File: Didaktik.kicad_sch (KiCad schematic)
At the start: 103 parts, among them J1 Conn_01x04_MountingPin, J2 AVR-ISP-6, SW1 SW_Push, SW10 SW_Push_45deg, SW11 SW_Push_45deg, SW12 SW_Push_45deg, SW13 SW_Push_45deg, SW14 SW_Push_45deg, SW15 SW_Push_45deg, SW16 SW_Push_45deg, SW17 SW_Push_45deg, SW18 SW_Push_45deg, SW19 SW_Push_45deg, SW2 SW_Push_45deg, SW20 SW_Push_45deg, SW21 SW_Push_45deg, SW22 SW_Push_45deg, SW23 SW_Push_45deg, SW24 SW_Push_45deg, SW25 SW_Push_45deg, SW26 SW_Push_45deg, SW27 SW_Push_45deg, SW28 SW_Push_45deg, SW29 SW_Push_45deg, SW3 SW_Push_45deg, SW30 SW_Push_45deg, SW31 SW_Push_45deg, SW32 SW_Push_45deg, SW33 SW_Push_45deg, SW34 SW_Push_45deg, SW35 SW_Push_45deg, SW36 SW_Push_45deg, SW37 SW_Push_45deg, SW38 SW_Push_45deg, SW39 SW_Push_45deg, SW4 SW_Push_45deg, SW40 SW_Push_45deg, SW41 SW_Push_45deg, SW5 SW_Push_45deg, SW6 SW_Push_45deg, SW7 SW_Push_45deg, SW8 SW_Push_45deg, SW9 SW_Push_45deg, U1 ATmega32U4-M, Y1 Crystal_GND24_Small

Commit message: added multi layout proto
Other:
- moved on the sheet: C1, C2, C5, C7, C8

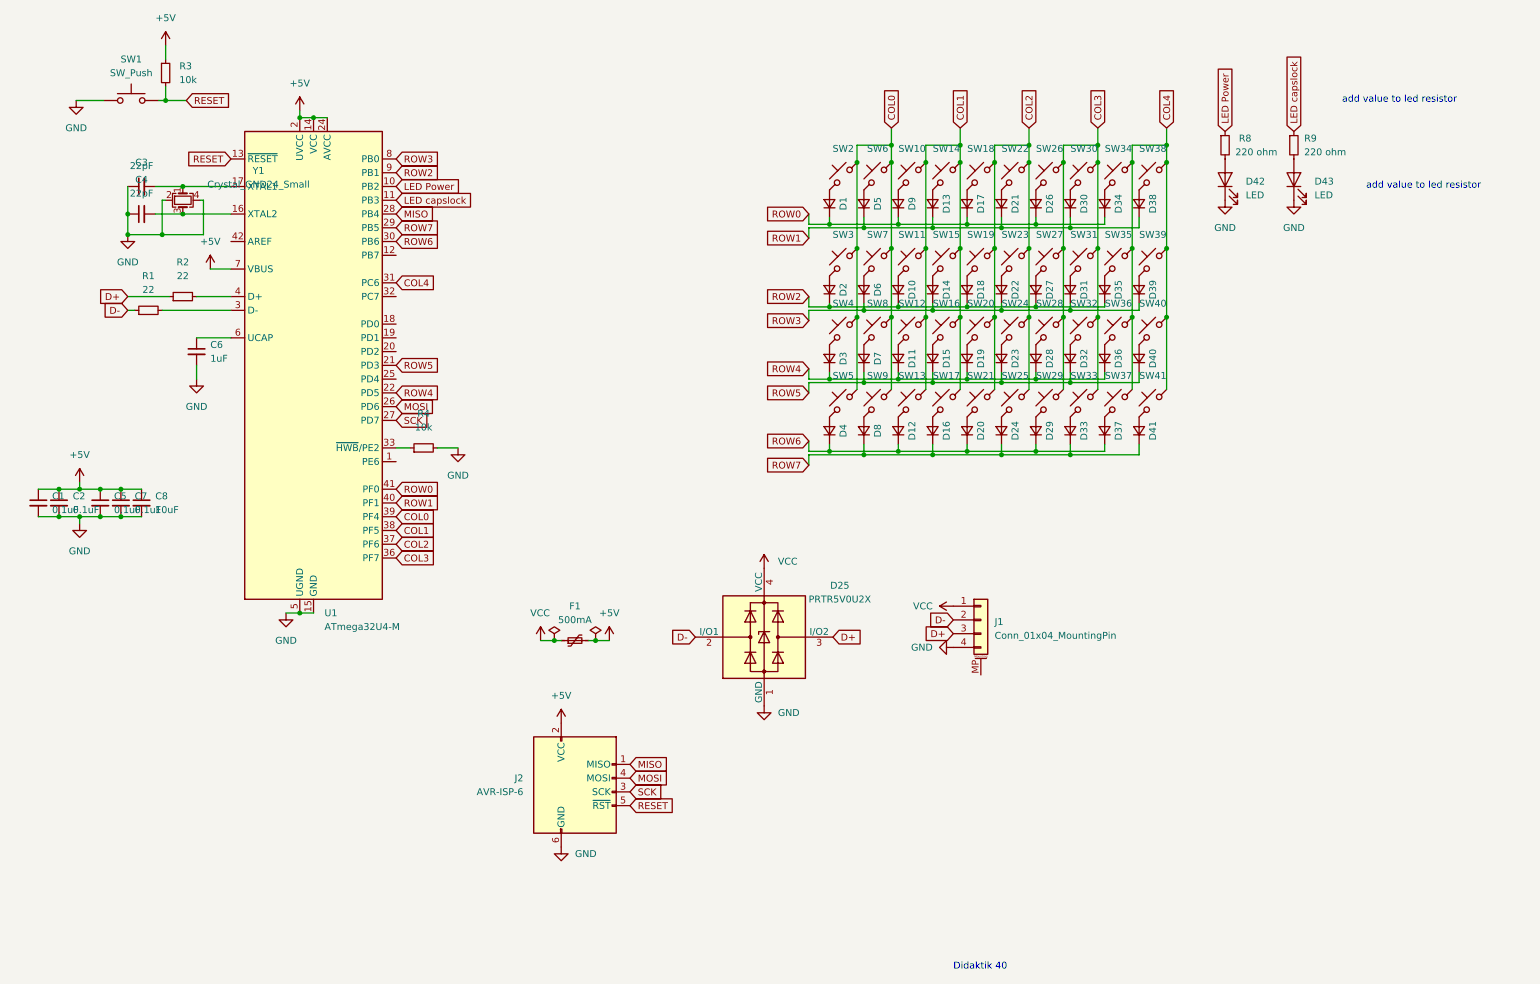
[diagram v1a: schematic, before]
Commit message: updated routing, created footprints for bottom row
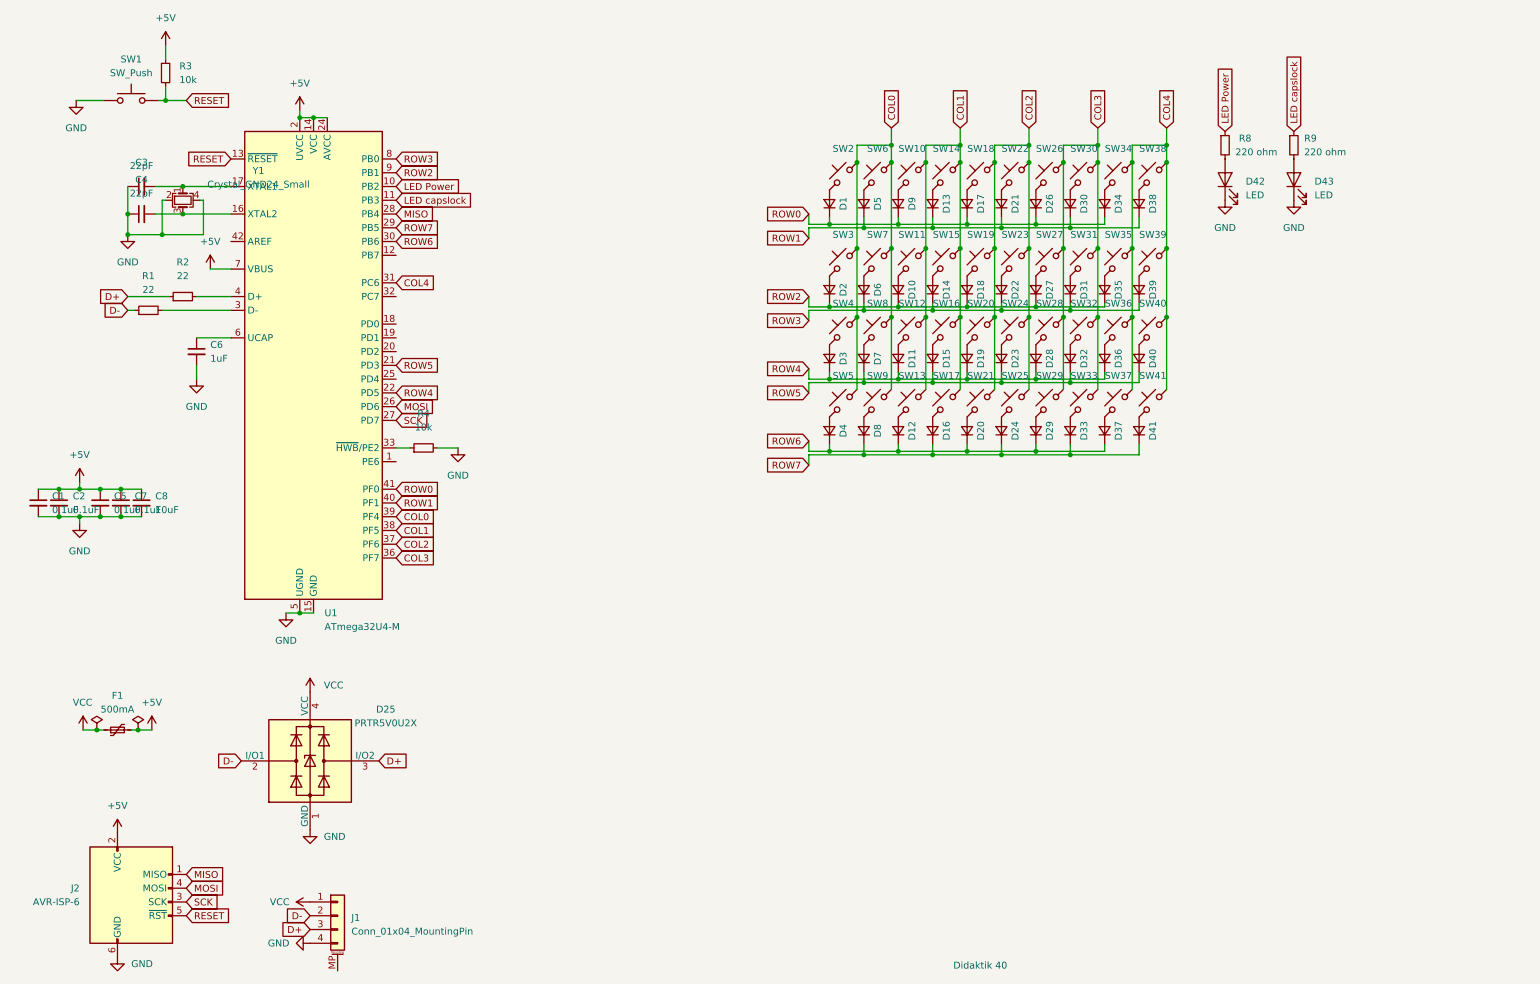
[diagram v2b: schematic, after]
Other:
- note removed: "add value to led resistor"
- moved on the sheet: D25, F1, J1, J2

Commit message: cleaned routing, added multilayout to schematics and laid out footprints under the pcb
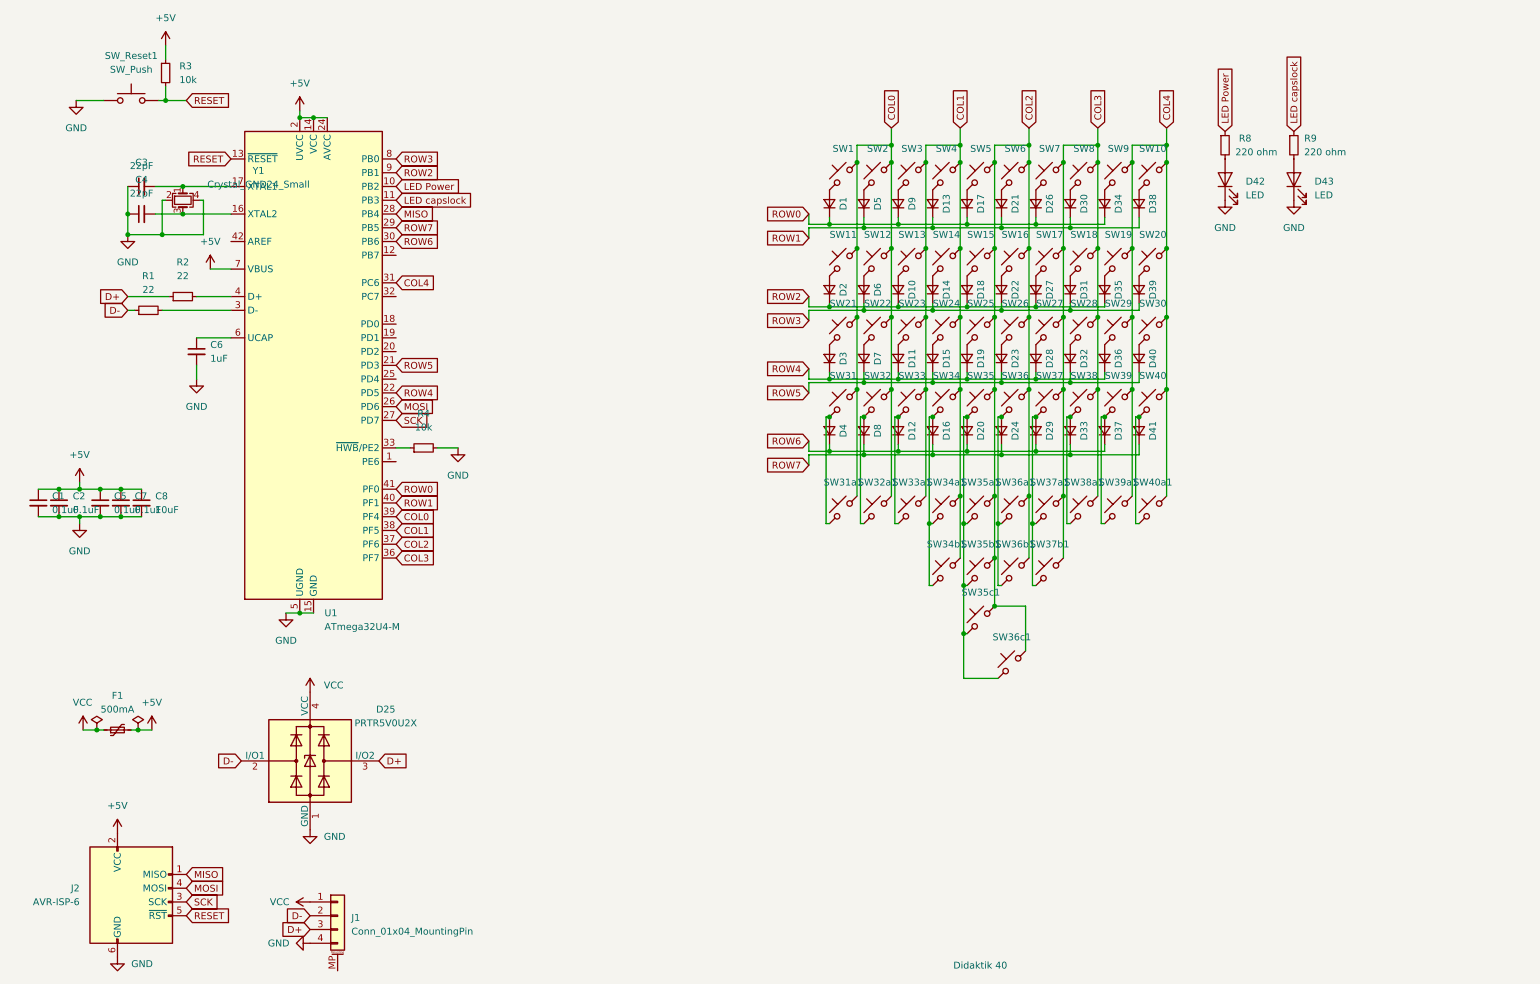
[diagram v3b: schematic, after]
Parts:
- added SW31a1, SW32a1, SW33a1, SW34a1, SW37a1, SW38a1, SW39a1, SW40a1: SW_Push_45deg, Keebio-Parts:MX-Alps-Choc-1U-NoLED, symbol Switch:SW_Push_45deg
- added SW34b1, SW37b1: SW_Push_45deg, Keebio-Parts:MX-Alps-Choc-3U-NoLED-StabFlip, symbol Switch:SW_Push_45deg
- added SW35a1, SW36a1: SW_Push_45deg, Keebio-Parts:MX-Alps-Choc-1.5U-NoLED, symbol Switch:SW_Push_45deg
- added SW35b1, SW36b1: SW_Push_45deg, Keebio-Parts:MX-Alps-Choc-2U-NoLED-StabFlip, symbol Switch:SW_Push_45deg
- added SW35c1: SW_Push_45deg, Keebio-Parts:MX-Alps-Choc-6U-NoLED-StabFlip, symbol Switch:SW_Push_45deg
- added SW36c1: SW_Push_45deg, Keebio-Parts:MX-Alps-Choc-7U-NoLED-StabFlip, symbol Switch:SW_Push_45deg
- SW31: renamed from SW5; footprint Keebio-Parts:MX-Alps-Choc-1U-NoLED -> Keebio-Parts:MX-Alps-Choc-1.5U-NoLED
- SW40: renamed from SW41; footprint Keebio-Parts:MX-Alps-Choc-1U-NoLED -> Keebio-Parts:MX-Alps-Choc-1.5U-NoLED
- renumbered SW2 to SW1, SW38 to SW10, SW3 to SW11, SW7 to SW12, SW11 to SW13, SW15 to SW14, SW19 to SW15, SW23 to SW16, SW27 to SW17, SW31 to SW18, SW35 to SW19, SW6 to SW2, SW39 to SW20, SW4 to SW21, SW8 to SW22, SW12 to SW23, SW16 to SW24, SW20 to SW25, SW24 to SW26, SW28 to SW27, SW32 to SW28, SW36 to SW29, SW10 to SW3, SW40 to SW30, SW9 to SW32, SW13 to SW33, SW17 to SW34, SW21 to SW35, SW25 to SW36, SW29 to SW37, SW33 to SW38, SW37 to SW39, SW14 to SW4, SW18 to SW5, SW22 to SW6, SW26 to SW7, SW30 to SW8, SW34 to SW9, SW1 to SW_Reset1
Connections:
- net COL0: now also SW31a1.1, SW32a1.1
- net COL1: now also SW33a1.1, SW34a1.1, SW34b1.1
- net COL2: now also SW35a1.1, SW35b1.1, SW35c1.1, SW36a1.1, SW36b1.1, SW36c1.1
- net COL3: now also SW37a1.1, SW37b1.1, SW38a1.1
- net COL4: now also SW39a1.1, SW40a1.1
- net at D37.2 (A), SW39.2: now also SW39a1.2
- net at D8.2 (A), SW32.2: now also SW32a1.2
- net at D33.2 (A), SW38.2: now also SW38a1.2
- net at D20.2 (A), SW35.2: now also SW35a1.2, SW35b1.2, SW35c1.2, SW36c1.2
- net at D41.2 (A), SW40.2: now also SW40a1.2
- net at D24.2 (A), SW36.2: now also SW36a1.2, SW36b1.2
- net at D12.2 (A), SW33.2: now also SW33a1.2
- net at D16.2 (A), SW34.2: now also SW34a1.2, SW34b1.2
- net at D29.2 (A), SW37.2: now also SW37a1.2, SW37b1.2
- net at D4.2 (A), SW31.2: now also SW31a1.2
